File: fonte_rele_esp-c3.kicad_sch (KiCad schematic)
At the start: 32 parts, among them J1 Screw_Terminal_01x03, J2 Conn_01x05_Pin, J3 Screw_Terminal_01x02, K1 G5LE-1, Q1 AO3400A, U1 AZ1117CH2-3.3, U2 HS-40012, U3 ESP32-C3-WROOM-02

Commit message: Atualizando fiduciais
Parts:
- added H4: MountingHole, MountingHole:MountingHole_2.2mm_M2, symbol Mechanical:MountingHole
- FID1, FID2, FID3: footprint (none) -> Fiducial:Fiducial_0.5mm_Mask1mm
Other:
- moved on the sheet: H2, H3
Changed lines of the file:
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@@
 			)
 		)
-		(property "Footprint" ""
+		(property "Footprint" "Fiducial:Fiducial_0.5mm_Mask1mm"
 			(at 176.53 147.32 0)
 			(hide yes)
@@
 	(symbol
 		(lib_id "Mechanical:MountingHole")
-		(at 247.65 147.32 0)
+		(at 212.09 153.67 0)
 		(unit 1)
 		(body_style 1)
@@
 		(fields_autoplaced yes)
 		(property "Reference" "H3"
-			(at 250.19 146.0499 0)
+			(at 214.63 152.3999 0)
 			(show_name no)
 			(do_not_autoplace no)
@@
 		)
 		(property "Value" "MountingHole"
-			(at 250.19 148.5899 0)
+			(at 214.63 154.9399 0)
 			(show_name no)
 			(do_not_autoplace no)
@@
 		)
 		(property "Footprint" "MountingHole:MountingHole_2.2mm_M2"
-			(at 247.65 147.32 0)
+			(at 212.09 153.67 0)
 			(hide yes)
 			(show_name no)
@@
 		)
 		(property "Datasheet" ""
-			(at 247.65 147.32 0)
+			(at 212.09 153.67 0)
 			(hide yes)
 			(show_name no)
@@
 		)
 		(property "Description" "Mounting Hole without connection"
-			(at 247.65 147.32 0)
+			(at 212.09 153.67 0)
 			(hide yes)
 			(show_name no)
@@
 			)
 		)
-		(property "Footprint" ""
+		(property "Footprint" "Fiducial:Fiducial_0.5mm_Mask1mm"
 			(at 163.83 147.32 0)
 			(hide yes)
@@
 			)
 		)
-		(property "Footprint" ""
+		(property "Footprint" "Fiducial:Fiducial_0.5mm_Mask1mm"
 			(at 191.77 147.32 0)
 			(hide yes)
@@
 	(symbol
 		(lib_id "Mechanical:MountingHole")
-		(at 229.87 147.32 0)
+		(at 237.49 147.32 0)
 		(unit 1)
 		(body_style 1)
@@
 		(fields_autoplaced yes)
 		(property "Reference" "H2"
-			(at 232.41 146.0499 0)
+			(at 240.03 146.0499 0)
 			(show_name no)
 			(do_not_autoplace no)
@@
 		)
 		(property "Value" "MountingHole"
-			(at 232.41 148.5899 0)
+			(at 240.03 148.5899 0)
 			(show_name no)
 			(do_not_autoplace no)
@@
 		)
 		(property "Footprint" "MountingHole:MountingHole_2.2mm_M2"
-			(at 229.87 147.32 0)
+			(at 237.49 147.32 0)
 			(hide yes)
 			(show_name no)
@@
 		)
 		(property "Datasheet" ""
-			(at 229.87 147.32 0)
+			(at 237.49 147.32 0)
 			(hide yes)
 			(show_name no)
@@
 		)
 		(property "Description" "Mounting Hole without connection"
-			(at 229.87 147.32 0)
+			(at 237.49 147.32 0)
 			(hide yes)
 			(show_name no)
@@
 					(unit 1)
 				)
+			)
+		)
+	)
+	(symbol
+		(lib_id "Mechanical:MountingHole")
+		(at 237.49 153.67 0)
+		(unit 1)
+		(body_style 1)
+		(exclude_from_sim no)
+		(in_bom no)
+		(on_board yes)
+		(in_pos_files yes)
+		(dnp no)
+		(fields_autoplaced yes)
+		(property "Reference" "H4"
+			(at 240.03 152.3999 0)
+			(show_name no)
+			(do_not_autoplace no)
+			(effects
+				(font
+					(size 1.27 1.27)
+				)
+				(justify left)
+			)
+		)
+		(property "Value" "MountingHole"
+			(at 240.03 154.9399 0)
+			(show_name no)
+			(do_not_autoplace no)
+			(effects
+				(font
+					(size 1.27 1.27)
+				)
+				(justify left)
+			)
+		)
+		(property "Footprint" "MountingHole:MountingHole_2.2mm_M2"
+			(at 237.49 153.67 0)
+			(hide yes)
+			(show_name no)
+			(do_not_autoplace no)
+			(effects
+				(font
+					(size 1.27 1.27)
+				)
+			)
+		)
+		(property "Datasheet" ""
+			(at 237.49 153.67 0)
+			(hide yes)
+			(show_name no)
+			(do_not_autoplace no)
+			(effects
+				(font
+					(size 1.27 1.27)
+				)
+			)
+		)
+		(property "Description" "Mounting Hole without connection"
+			(at 237.49 153.67 0)
+			(hide yes)
+			(show_name no)
+			(do_not_autoplace no)
+			(effects
+				(font
+					(size 1.27 1.27)
+				)
+			)
+		)
+		(instances
+			(project "fonte_rele_esp-c3"
+				(path "/994e14a8-d3ff-4177-8421-d15111a8b3ec"
+					(reference "H4")
+					(unit 1)
+				)

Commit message: Ajusta posição do símbolo de terra no esquemático
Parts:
- J2: footprint Connector_PinHeader_1.00mm:PinHeader_1x05_P1.00mm_Vertical -> Connector_PinHeader_2.54mm:PinHeader_1x05_P2.54mm_Vertical
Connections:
- net Earth: now also J1.2 (Pin_2); no longer J1.1 (Pin_1)
- net N: now also J1.1 (Pin_1); no longer J1.2 (Pin_2)
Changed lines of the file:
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@@
 	(wire
 		(pts
-			(xy 55.88 39.37) (xy 55.88 44.45)
+			(xy 46.99 46.99) (xy 46.99 48.26)
 		)
 		(stroke
@@
 	(wire
 		(pts
-			(xy 55.88 44.45) (xy 39.37 44.45)
-		)
-		(stroke
-			(width 0)
-			(type default)
-		)
-	)
-	(wire
-		(pts
 			(xy 120.65 46.99) (xy 124.46 46.99)
 		)
@@
 	(wire
 		(pts
-			(xy 46.99 46.99) (xy 46.99 50.8)
-		)
-		(stroke
-			(width 0)
-			(type default)
-		)
-	)
-	(wire
-		(pts
 			(xy 149.86 116.84) (xy 149.86 118.11)
 		)
@@
 	(wire
 		(pts
+			(xy 52.07 44.45) (xy 39.37 44.45)
+		)
+		(stroke
+			(width 0)
+			(type default)
+		)
+	)
+	(wire
+		(pts
 			(xy 207.01 49.53) (xy 207.01 52.07)
 		)
@@
 	(wire
 		(pts
+			(xy 52.07 46.99) (xy 52.07 44.45)
+		)
+		(stroke
+			(width 0)
+			(type default)
+		)
+	)
+	(wire
+		(pts
 			(xy 220.98 118.11) (xy 224.79 118.11)
 		)
@@
 	)
 	(symbol
+		(lib_id "power:Earth")
+		(at 52.07 46.99 0)
+		(unit 1)
+		(body_style 1)
+		(exclude_from_sim no)
+		(in_bom yes)
+		(on_board yes)
+		(in_pos_files yes)
+		(dnp no)
+		(fields_autoplaced yes)
+		(property "Reference" "#PWR03"
+			(at 52.07 53.34 0)
+			(hide yes)
+			(show_name no)
+			(do_not_autoplace no)
+			(effects
+				(font
+					(size 1.27 1.27)
+				)
+			)
+		)
+		(property "Value" "Earth"
+			(at 52.07 52.07 0)
+			(show_name no)
+			(do_not_autoplace no)
+			(effects
+				(font
+					(size 1.27 1.27)
+				)
+			)
+		)
+		(property "Footprint" ""
+			(at 52.07 46.99 0)
+			(hide yes)
+			(show_name no)
+			(do_not_autoplace no)
+			(effects
+				(font
+					(size 1.27 1.27)
+				)
+			)
+		)
+		(property "Datasheet" ""
+			(at 52.07 46.99 0)
+			(hide yes)
+			(show_name no)
+			(do_not_autoplace no)
+			(effects
+				(font
+					(size 1.27 1.27)
+				)
+			)
+		)
+		(property "Description" "Power symbol creates a global label with name \"Earth\""
+			(at 52.07 46.99 0)
+			(hide yes)
+			(show_name no)
+			(do_not_autoplace no)
+			(effects
+				(font
+					(size 1.27 1.27)
+				)
+			)
+		)
+		(pin "1"
+		)
+		(instances
+			(project "fonte_rele_esp-c3"
+				(path "/994e14a8-d3ff-4177-8421-d15111a8b3ec"
+					(reference "#PWR03")
+					(unit 1)
+				)
+			)
+		)
+	)
+	(symbol
 		(lib_id "PCM_JLCPCB-Resistors:0603,1kΩ")
 		(at 46.99 163.83 270)
@@
 	)
 	(symbol
-		(lib_id "power:Earth")
-		(at 46.99 50.8 0)
-		(unit 1)
-		(body_style 1)
-		(exclude_from_sim no)
-		(in_bom yes)
-		(on_board yes)
-		(in_pos_files yes)
-		(dnp no)
-		(fields_autoplaced yes)
-		(property "Reference" "#PWR03"
-			(at 46.99 57.15 0)
-			(hide yes)
-			(show_name no)
-			(do_not_autoplace no)
-			(effects
-				(font
-					(size 1.27 1.27)
-				)
-			)
-		)
-		(property "Value" "Earth"
-			(at 46.99 55.88 0)
-			(show_name no)
-			(do_not_autoplace no)
-			(effects
-				(font
-					(size 1.27 1.27)
-				)
-			)
-		)
-		(property "Footprint" ""
-			(at 46.99 50.8 0)
-			(hide yes)
-			(show_name no)
-			(do_not_autoplace no)
-			(effects
-				(font
-					(size 1.27 1.27)
-				)
-			)
-		)
-		(property "Datasheet" ""
-			(at 46.99 50.8 0)
-			(hide yes)
-			(show_name no)
-			(do_not_autoplace no)
-			(effects
-				(font
-					(size 1.27 1.27)
-				)
-			)
-		)
-		(property "Description" "Power symbol creates a global label with name \"Earth\""
-			(at 46.99 50.8 0)
-			(hide yes)
-			(show_name no)
-			(do_not_autoplace no)
-			(effects
-				(font
-					(size 1.27 1.27)
-				)
-			)
-		)
-		(pin "1"
-		)
-		(instances
-			(project "fonte_rele_esp-c3"
-				(path "/994e14a8-d3ff-4177-8421-d15111a8b3ec"
-					(reference "#PWR03")
-					(unit 1)
-				)
-			)
-		)
-	)
-	(symbol
 		(lib_id "power:GND")
 		(at 168.91 110.49 0)
@@
 	(symbol
 		(lib_id "power:AC")
-		(at 55.88 39.37 0)
+		(at 46.99 48.26 180)
 		(unit 1)
 		(body_style 1)
@@
 		(in_pos_files yes)
 		(dnp no)
-		(fields_autoplaced yes)
 		(property "Reference" "#PWR02"
-			(at 55.88 41.91 0)
+			(at 46.99 45.72 0)
 			(hide yes)
 			(show_name no)
@@
 		)
 		(property "Value" "N"
-			(at 55.88 31.75 0)
+			(at 43.688 51.816 0)
 			(show_name no)
 			(do_not_autoplace no)
@@
 		)
 		(property "Footprint" ""
-			(at 55.88 39.37 0)
+			(at 46.99 48.26 0)
 			(hide yes)
 			(show_name no)
@@
 		)
 		(property "Datasheet" ""
-			(at 55.88 39.37 0)
+			(at 46.99 48.26 0)
 			(hide yes)
 			(show_name no)
@@
 		)
 		(property "Description" "Power symbol creates a global label with name \"N\""
-			(at 55.88 39.37 0)
+			(at 46.99 48.26 0)
 			(hide yes)
 			(show_name no)
@@
 			)
 		)
-		(property "Footprint" "Connector_PinHeader_1.00mm:PinHeader_1x05_P1.00mm_Vertical"
+		(property "Footprint" "Connector_PinHeader_2.54mm:PinHeader_1x05_P2.54mm_Vertical"
 			(at 48.26 92.71 0)
 			(hide yes)

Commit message: Move controle do relé de GPIO9 (strapping) pra GPIO0 e atualiza layout da PCB
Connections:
- net RELE: now also U3.10 (IO10); no longer U3.17 (IO1)
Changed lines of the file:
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@@
-	(wire
-		(pts
-			(xy 129.54 113.03) (xy 129.54 115.57)
-		)
-		(stroke
-			(width 0)
-			(type default)
-		)
-	)
 	(wire
 		(pts
@@
 		(pts
 			(xy 106.68 106.68) (xy 111.76 106.68)
+		)
+		(stroke
+			(width 0)
+			(type default)
+		)
+	)
+	(wire
+		(pts
+			(xy 152.4 113.03) (xy 152.4 115.57)
 		)
 		(stroke
@@
 		)
 	)
-	(label "RELE"
-		(at 129.54 115.57 270)
-		(effects
-			(font
-				(size 1.27 1.27)
-			)
-			(justify right bottom)
-		)
-	)
 	(label "DRAIN"
 		(at 210.82 118.11 180)
@@
 		(effects
 			(font
+				(size 1.27 1.27)
+			)
+			(justify right bottom)
+		)
+	)
+	(label "RELE"
+		(at 152.4 115.57 270)
+		(effects
+			(font

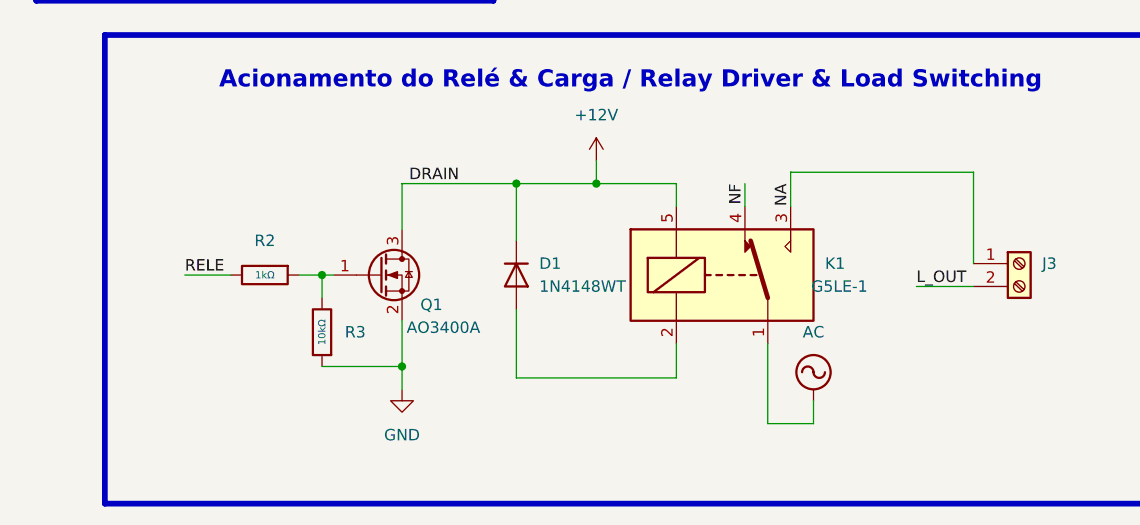
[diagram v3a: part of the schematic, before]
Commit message: Ajusta J3 (L_IN/L_OUT) e layout de PCB do driver do relé
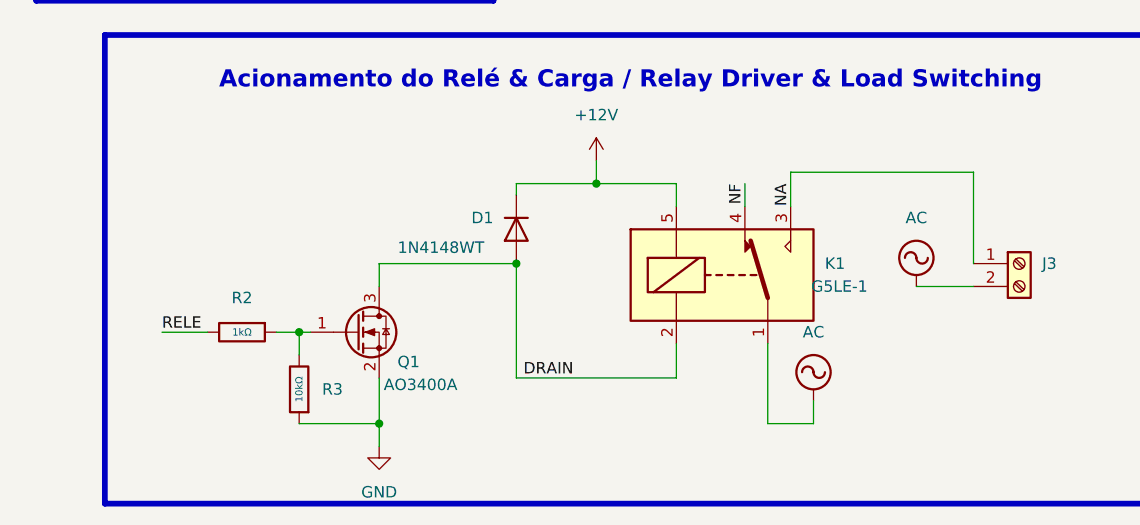
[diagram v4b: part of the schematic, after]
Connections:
- net L_OUT is gone; now on net AC: J3.2 (Pin_2)
- net +12V: no longer Q1.3 (D), R6.1
- net DRAIN: now reaches D1.2 (A), K1.2
- net DRAIN: now also Q1.3 (D), R6.1
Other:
- moved on the sheet: D1, Q1, R2, R3

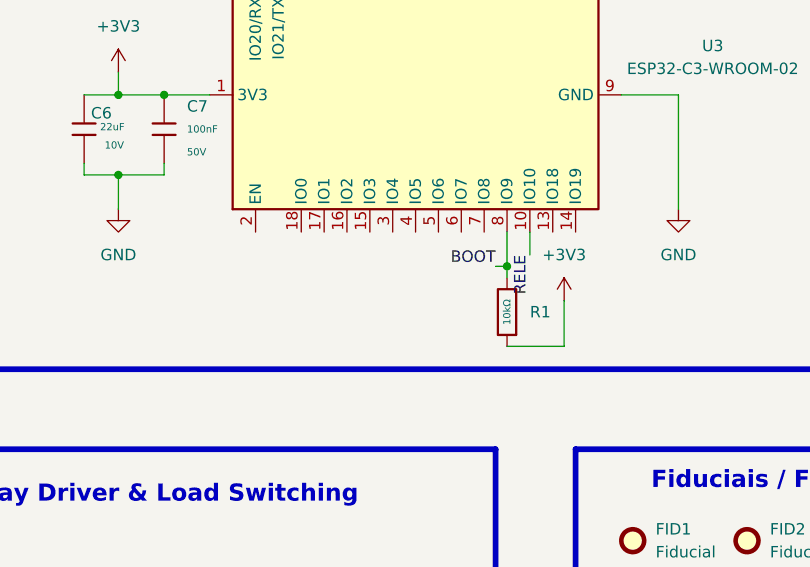
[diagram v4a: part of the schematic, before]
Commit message: Adiciona pull-up de 10k no EN do ESP32-C3 (R7)
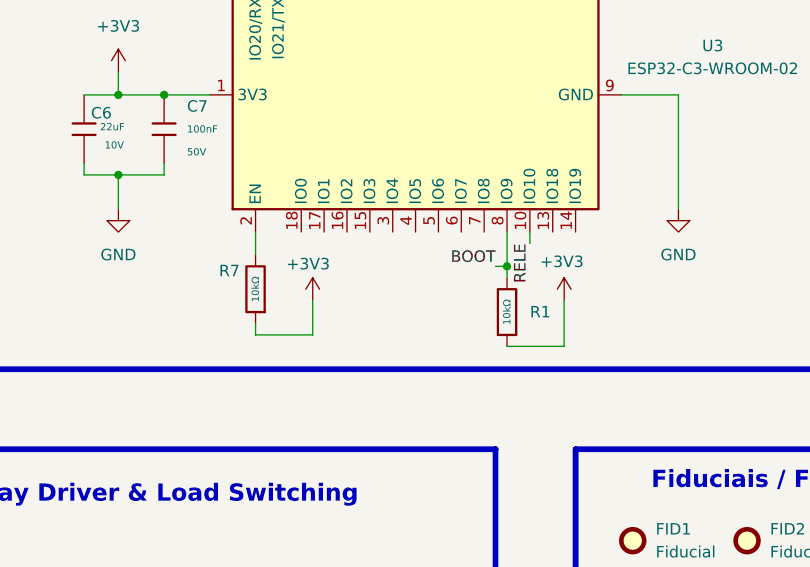
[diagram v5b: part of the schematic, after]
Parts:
- added R7: 10kΩ, Resistor_SMD:R_0603_1608Metric, symbol PCM_JLCPCB-Resistors:0603,10kΩ
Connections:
- net +3V3: now also R7.1
- net at U3.2 (EN): now also R7.2

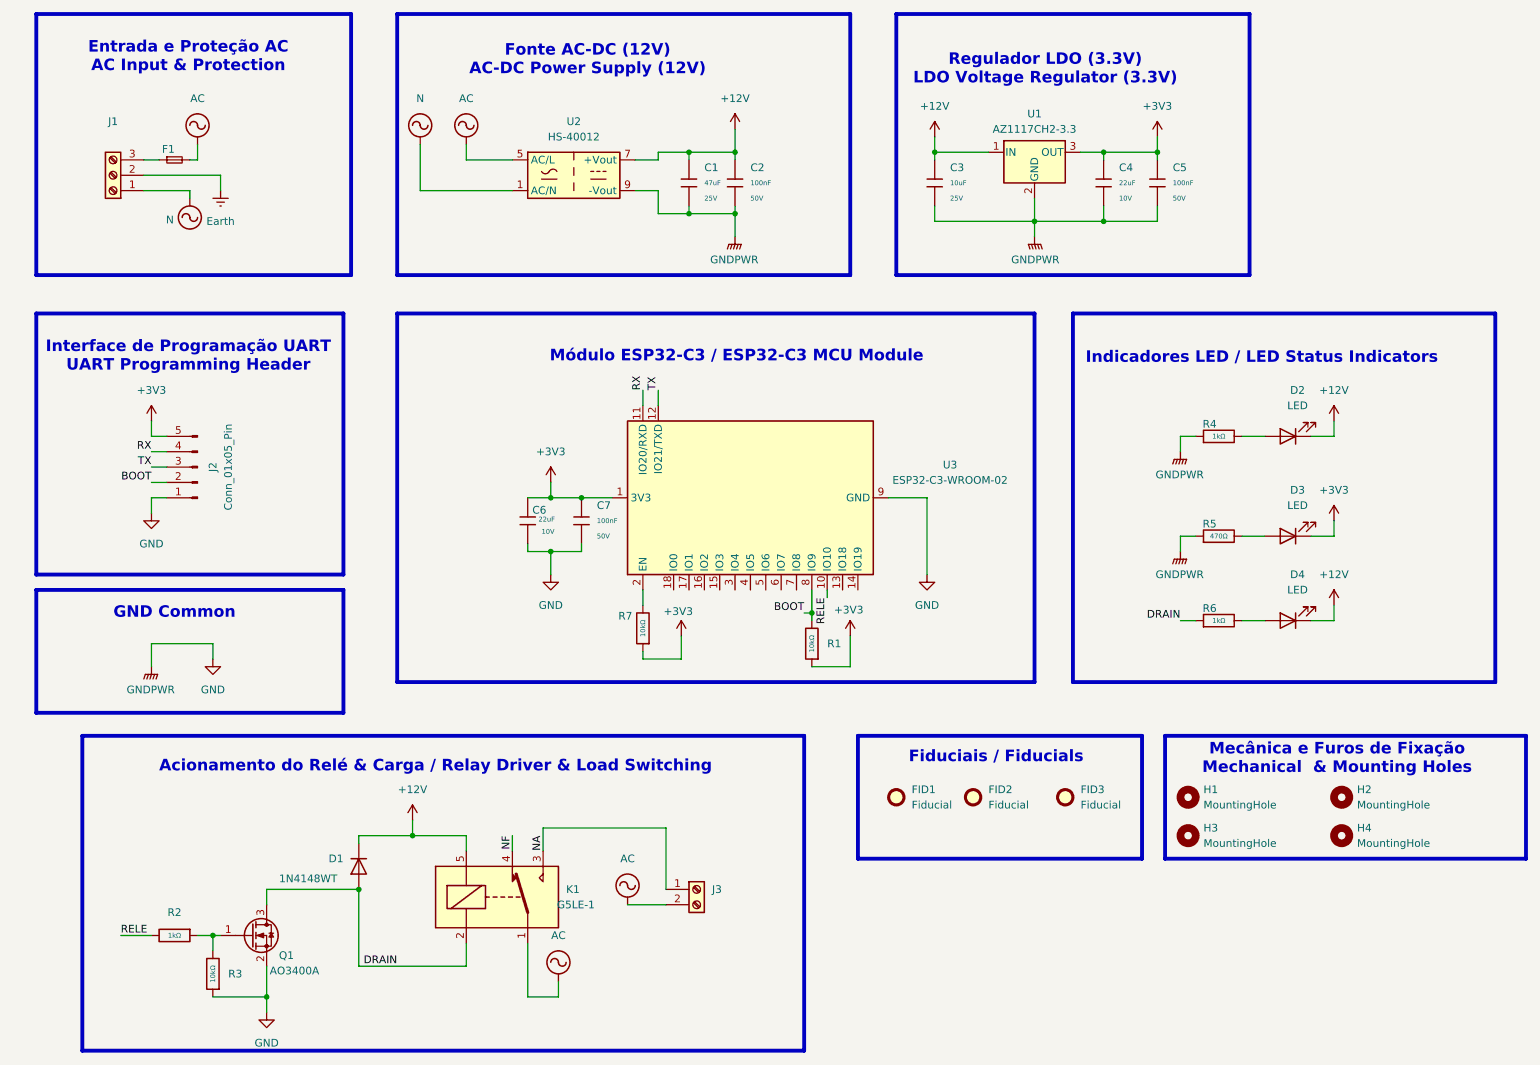
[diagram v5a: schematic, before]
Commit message: Atualiza esquematico e PCB do fonte_rele_esp-c3
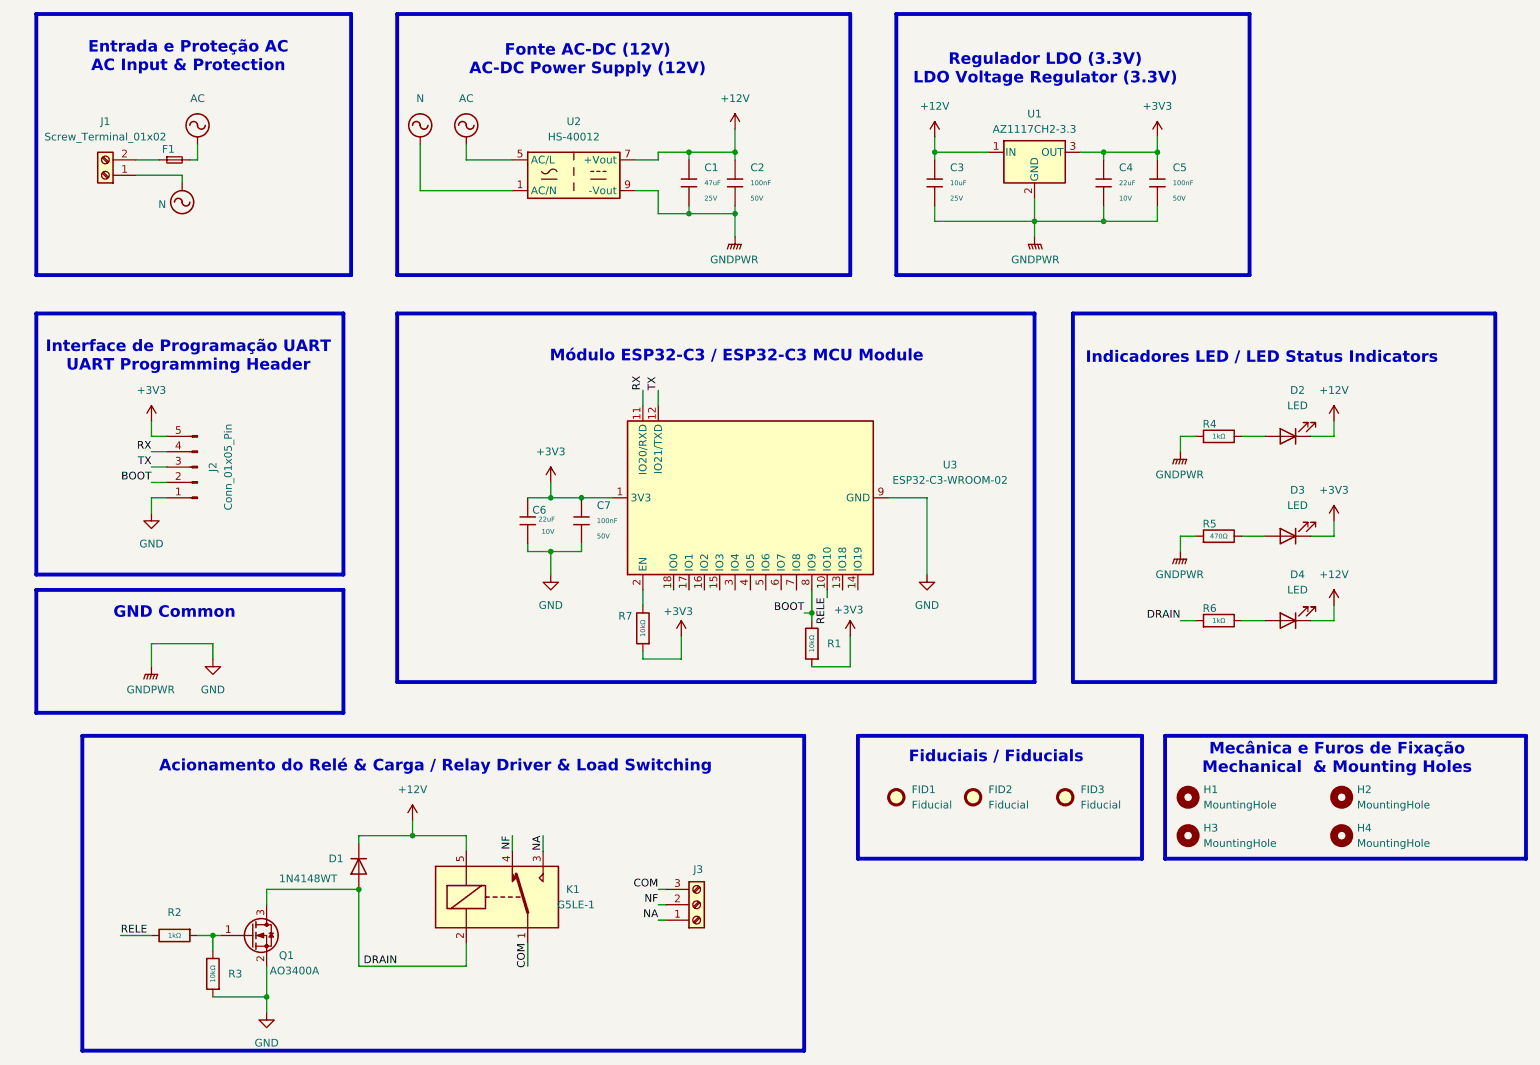
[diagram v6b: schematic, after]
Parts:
- removed J1: Screw_Terminal_01x03, TerminalBlock_MetzConnect:TerminalBlock_MetzConnect_Type011_RT05503HBLC_1x03_P5.00mm_Horizontal, symbol Connector:Screw_Terminal_01x03
- removed J3: Screw_Terminal_01x02, TerminalBlock:TerminalBlock_MaiXu_MX126-5.0-02P_1x02_P5.00mm, symbol Connector:Screw_Terminal_01x02
- added J1: Screw_Terminal_01x02, TerminalBlock_MetzConnect:TerminalBlock_MetzConnect_Type094_RT03502HBLU_1x02_P5.00mm_Horizontal, symbol Connector:Screw_Terminal_01x02
- added J3: Screw_Terminal_01x03, TerminalBlock_MetzConnect:TerminalBlock_MetzConnect_Type094_RT03503HBLU_1x03_P5.00mm_Horizontal, symbol Connector:Screw_Terminal_01x03
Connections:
- net AC: no longer K1.1
- net N: now also J1.1 (Pin_1)
- net NA: now also J3.1 (Pin_1)
- net NF: now also J3.2 (Pin_2)
- net at F1.1: now also J1.2 (Pin_2)
- new net COM: J3.3 (Pin_3), K1.1

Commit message: Adiciona gerbers, atualiza PCB e documenta jumper externo do COM do rele
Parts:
- F1: footprint Fuse:Fuseholder_Cylinder-5x20mm_Bulgin_FX0456_Vertical_Closed -> Fuse:Fuseholder_Littelfuse_Nano2_157x
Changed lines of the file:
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@@
 			)
 		)
-		(property "Footprint" "Fuse:Fuseholder_Cylinder-5x20mm_Bulgin_FX0456_Vertical_Closed"
+		(property "Footprint" "Fuse:Fuseholder_Littelfuse_Nano2_157x"
 			(at 44.45 41.91 0)
 			(hide yes)

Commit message: Atualiza projeto KiCad e imagens da PCB
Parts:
- J1, J2, J3: now left out of the parts list
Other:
- note removed: "GND Common"
